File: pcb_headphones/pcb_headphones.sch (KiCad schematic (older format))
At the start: 32 parts, among them J1 CONN_01X03, J2 CONN_01X03, J3 CONN_01X03, J4 CONN_01X02, Q1 TIP121, U1 MC34063, U2 TDA2822M

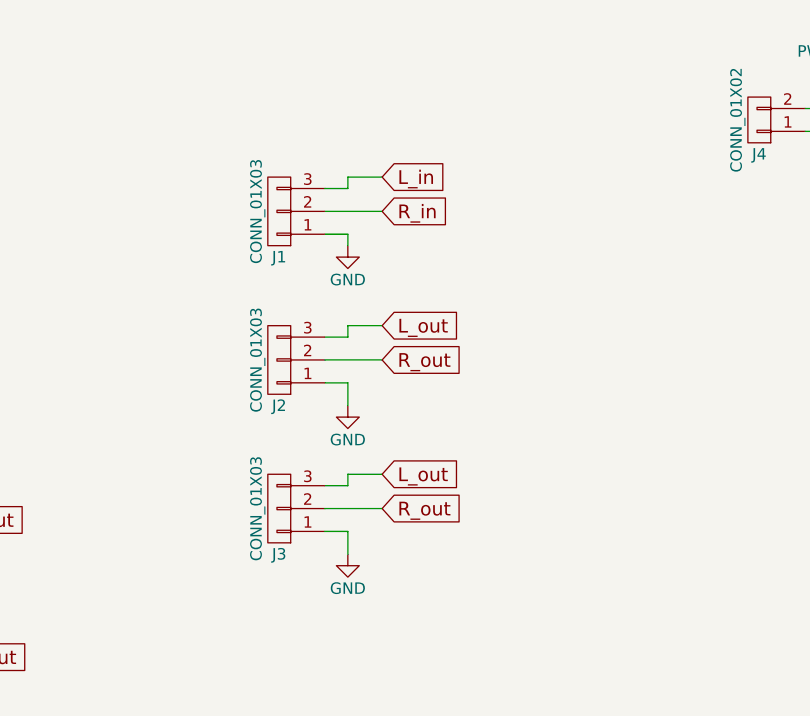
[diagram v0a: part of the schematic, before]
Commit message: Reorganizing connectors
Signed-off-by: Jan Losinski <losinski@wh2.tu-dresden.de>
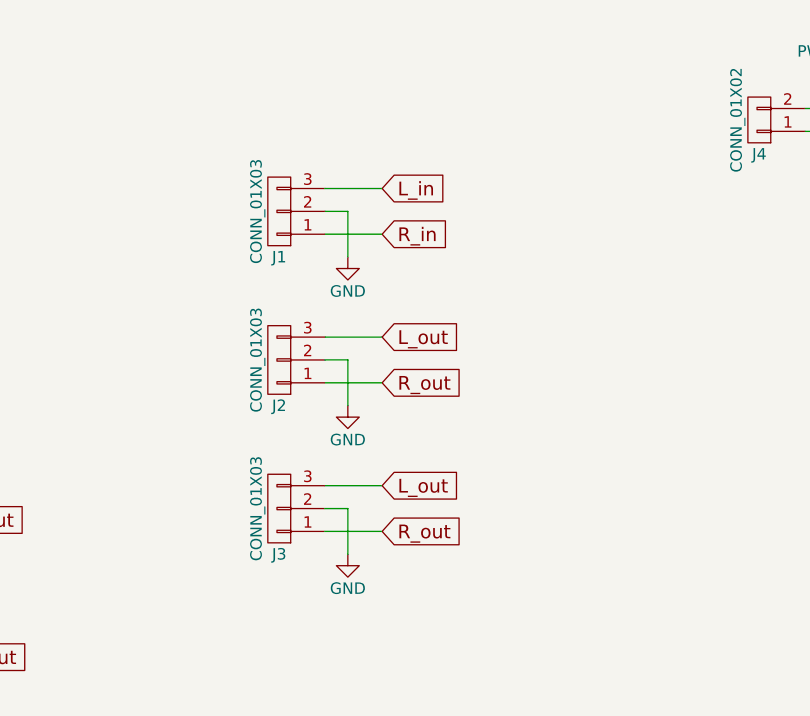
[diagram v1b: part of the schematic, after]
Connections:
- net GND: now also J1.2 (P2), J2.2 (P2), J3.2 (P2); no longer J1.1 (P1), J2.1 (P1), J3.1 (P1)
- net R_in: now also J1.1 (P1); no longer J1.2 (P2)
- net R_out: now also J2.1 (P1), J3.1 (P1); no longer J2.2 (P2), J3.2 (P2)
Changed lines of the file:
@@
 LIBS:valves
 LIBS:w_analog
+LIBS:pcb_headphones-cache
 EELAYER 25 0
 EELAYER END
@@
 	-1   0    0    1
 $EndComp
-Text GLabel 7350 4800 2    60   Input ~ 0
+Text GLabel 7350 4850 2    60   Input ~ 0
 L_out
-Text GLabel 7350 4950 2    60   Input ~ 0
+Text GLabel 7350 5050 2    60   Input ~ 0
 R_out
-Text GLabel 7350 4150 2    60   Input ~ 0
+Text GLabel 7350 4200 2    60   Input ~ 0
 L_out
-Text GLabel 7350 4300 2    60   Input ~ 0
+Text GLabel 7350 4400 2    60   Input ~ 0
 R_out
 Wire Wire Line
-	7350 4300 7100 4300
-Wire Wire Line
-	7100 4200 7200 4200
-Wire Wire Line
-	7200 4200 7200 4150
-Wire Wire Line
-	7200 4150 7350 4150
-Wire Wire Line
-	7100 4850 7200 4850
-Wire Wire Line
-	7200 4850 7200 4800
-Wire Wire Line
-	7200 4800 7350 4800
-Wire Wire Line
-	7350 4950 7100 4950
+	7100 4200 7350 4200
+Wire Wire Line
+	7100 4850 7350 4850
 $Comp
 L GND #PWR07
@@
 $EndComp
 Wire Wire Line
-	7200 4500 7200 4400
-Wire Wire Line
-	7200 4400 7100 4400
-Wire Wire Line
-	7200 5150 7200 5050
-Wire Wire Line
-	7200 5050 7100 5050
+	7200 4300 7200 4500
+Wire Wire Line
+	7200 4950 7200 5150
 $Comp
 L GND #PWR09
 U 1 1 592EC422
-P 7200 3800
-F 0 "#PWR09" H 7200 3550 50  0001 C CNN
-F 1 "GND" H 7200 3650 50  0000 C CNN
-F 2 "" H 7200 3800 50  0001 C CNN
-F 3 "" H 7200 3800 50  0001 C CNN
-	1    7200 3800
-	1    0    0    -1
-$EndComp
-Wire Wire Line
-	7100 3750 7200 3750
-Wire Wire Line
-	7200 3750 7200 3800
-Text GLabel 7350 3500 2    60   Input ~ 0
+P 7200 3850
+F 0 "#PWR09" H 7200 3600 50  0001 C CNN
+F 1 "GND" H 7200 3700 50  0000 C CNN
+F 2 "" H 7200 3850 50  0001 C CNN
+F 3 "" H 7200 3850 50  0001 C CNN
+	1    7200 3850
+	1    0    0    -1
+$EndComp
+Wire Wire Line
+	7200 3650 7200 3850
+Text GLabel 7350 3550 2    60   Input ~ 0
 L_in
-Text GLabel 7350 3650 2    60   Input ~ 0
+Text GLabel 7350 3750 2    60   Input ~ 0
 R_in
 Wire Wire Line
-	7350 3650 7100 3650
-Wire Wire Line
-	7100 3550 7200 3550
-Wire Wire Line
-	7200 3550 7200 3500
-Wire Wire Line
-	7200 3500 7350 3500
+	7100 3550 7350 3550
 $Comp
 L CONN_01X02 J4
@@
 Connection ~ 9750 3200
 Connection ~ 9350 3300
+Wire Wire Line
+	7100 4950 7200 4950
+Wire Wire Line
+	7100 3650 7200 3650
+Wire Wire Line
+	7350 3750 7100 3750
+Wire Wire Line
+	7350 5050 7100 5050
+Wire Wire Line
+	7200 4300 7100 4300
+Wire Wire Line
+	7350 4400 7100 4400
 $EndSCHEMATC
